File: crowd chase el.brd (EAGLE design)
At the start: 78.7 x 72.4 mm, 27 parts, among them IC2 PIC18F1220P, U4 TRIAC

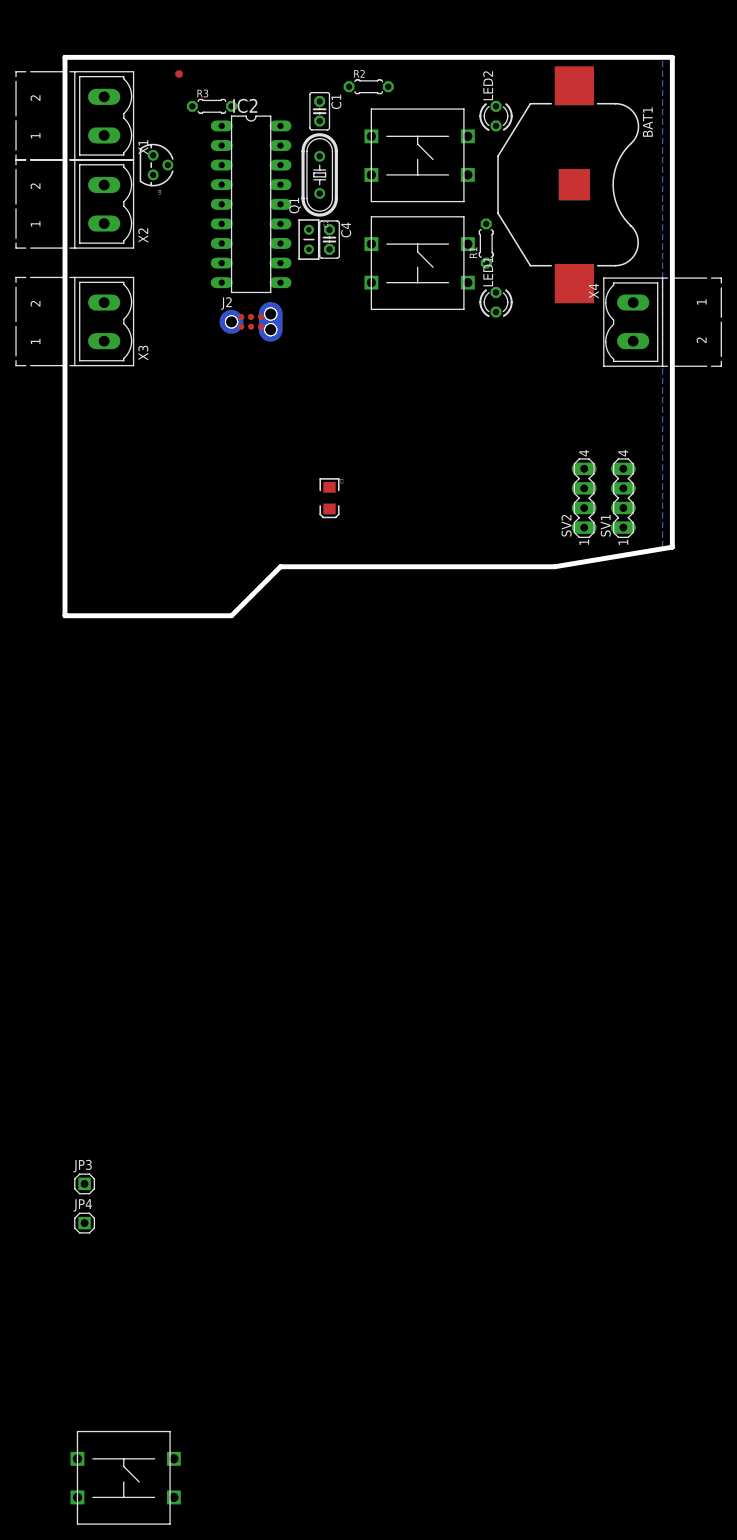
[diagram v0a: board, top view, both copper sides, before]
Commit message: No more airwires
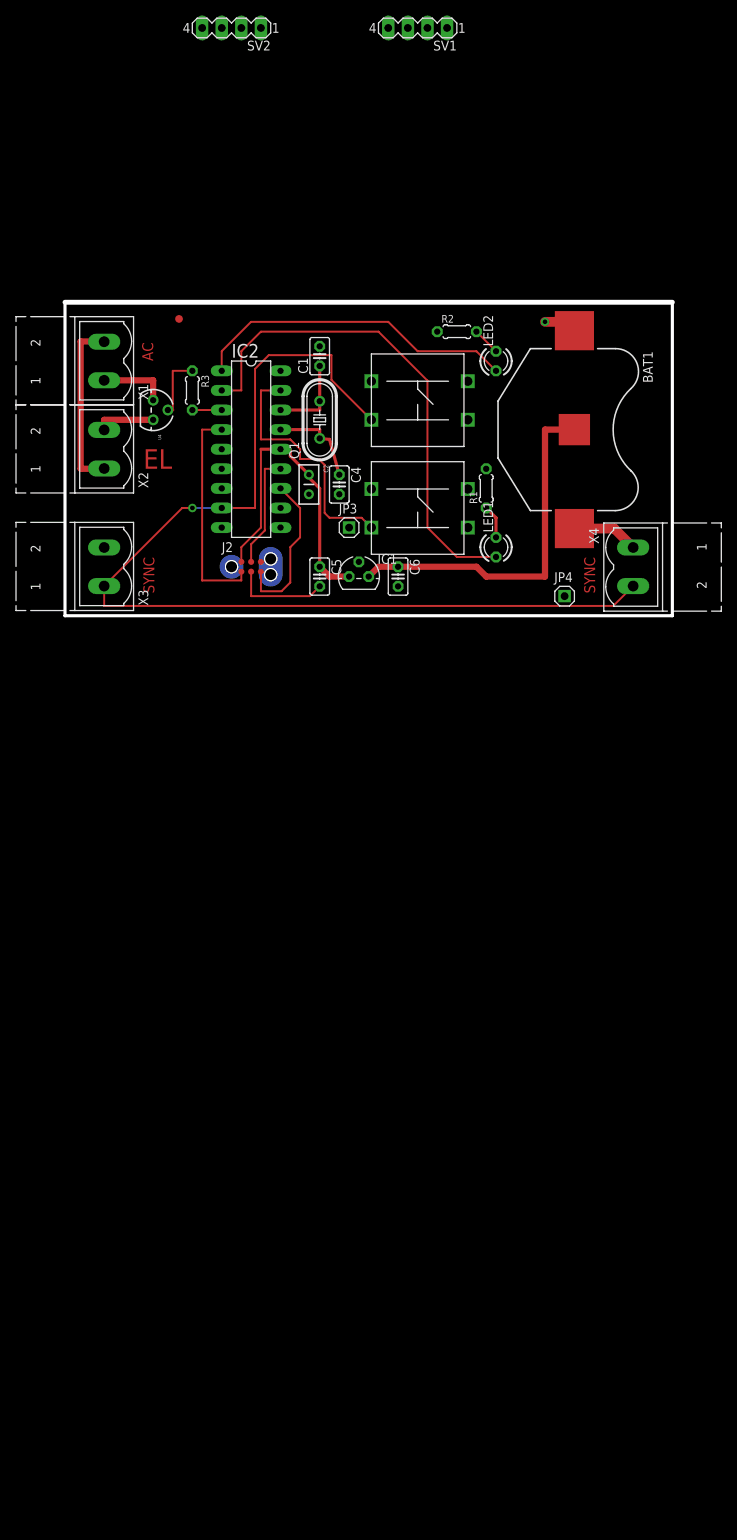
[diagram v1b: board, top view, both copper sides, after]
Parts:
- removed C3: 10uF, SparkFun:EIA3216
- removed U$7: 12MMTACT_MJTP1212, chasetron:MJTP1212
- added C5, C6: 1uF, rcl:C025-025X050
- added IC1: 7805L, linear:TO92
- moved JP4 102.4 mm to (64.8, 2.54)
- moved JP3 91.7 mm to (36.8, 11.4)
- moved SV2 76.2 mm to (21.6, 76.2), turned to 180 degrees
- moved SV1 66.5 mm to (45.7, 76.2), turned to 180 degrees
- moved R3 36.9 mm to (16.5, 29.2), turned to 270 degrees
- moved R2 33.7 mm to (50.8, 36.8)
- moved C4 31.8 mm to (35.6, 17.0)
- moved BAT1 31.8 mm to (66.0, 24.1)
- moved IC2 31.8 mm to (24.1, 21.6)
- moved X2 31.8 mm to (5.08, 21.6)
- moved C1 31.8 mm to (33.0, 33.7), turned to 90 degrees
- moved J2 31.8 mm to (21.6, 6.35)
- moved LED1 31.8 mm to (55.9, 8.89)
- moved Q1 31.8 mm to (33.0, 25.4)
- moved U$6 31.8 mm to (45.7, 14.0)
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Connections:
- new net DEVICE_MAX_SET: IC2.17, U$6.P2A
- new net MAX_LED: IC2.1, LED2.A
- new net N$4: BAT1.2, C6.1, IC1.3
- new net N$8: IC2.9
- new net NUM_LED: IC2.2, LED1.A
- net DEVICE_NUM_SET: now also IC2.8
- net EL_C: now also IC2.3
- net GND: now also C5.2, C6.2, IC1.2, R1.2, R2.1, U$6.P1A; no longer C3.C
- net VDD: now also C5.1, IC1.1, JP3.1; no longer BAT1.2, C3.A
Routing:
- net DEVICE_NUM_SET: track 0.00 -> 135.2 mm, vias 0 -> 1
- net NUM_LED: track 0.00 -> 65.0 mm
- net N$4: track 0.00 -> 46.8 mm
- net MAX_LED: track 0.00 -> 42.3 mm
- net VDD: track 0.00 -> 40.6 mm
- net DEVICE_MAX_SET: track 0.00 -> 32.4 mm
- net N$1: track 0.00 -> 28.3 mm
- net GND: track 0.00 -> 25.0 mm, vias 0 -> 1
- net HV1: track 0.00 -> 22.6 mm
- net ICSP_CLK: track 0.00 -> 20.6 mm
- net ICSP_DATA: track 0.00 -> 14.8 mm
- net N$2: track 0.00 -> 12.2 mm
- net N$3: track 0.00 -> 10.8 mm
- net HVGND1: track 0.00 -> 8.93 mm
- net N$10: track 0.00 -> 8.25 mm
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- removed copper zone on layer 1, net GND
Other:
- board size 78.7 x 72.4 mm -> 78.7 x 40.6 mm
- board text added: "AC"
- board text added: "Blake Robertson"
- board text added: "EL"
- board text added: "SYNC"
- board text removed: "Ryan Owens"

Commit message: v1.0 -- Fabbed Version
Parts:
- added LED3: (no value), led:LED3MM
- added R4: (no value), resistor:0204/5
- added U1: TRIAC, SparkFun:TO-92
- IC1: value 7805L -> REG
- moved SV2 64.1 mm to (6.35, 14.0)
- moved JP4 46.2 mm to (19.1, 8.89)
- moved SV1 38.9 mm to (53.3, 38.1)
- moved JP3 1.80 mm to (35.6, 10.2)
- moved C1 1.42 mm to (34.3, 33.0), turned to 0 degrees
- moved C2 1.27 mm to (31.6, 17.0)
- moved R2 1.27 mm to (50.8, 35.6)
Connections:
- removed net N$4: BAT1.2, C6.1, IC1.3
- new net N$12: SV2.1, U1.3
- new net N$13: SV2.3, U1.1
- new net N$14: IC2.6, U1.2
- new net N$7: IC2.7, LED3.A
- new net N$9: BAT1.3, C6.1, IC1.3
- net GND: now also BAT1.2, LED3.K; no longer BAT1.3
- net N$1: now also R4.1
- net N$8: now also JP4.1
- net VDD: now also R4.2
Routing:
- net N$4: track 46.8 -> 0.00 mm
- net N$9: track 0.00 -> 30.3 mm
- net N$14: track 0.00 -> 14.4 mm, vias 0 -> 2
- net N$13: track 0.00 -> 9.20 mm
- net VDD: track 40.6 -> 49.2 mm
- net N$7: track 0.00 -> 7.62 mm, vias 0 -> 1
- net DEVICE_NUM_SET: track 135.2 -> 142.2 mm
- net HV1: track 22.6 -> 27.7 mm, vias 0 -> 1
- net N$1: track 28.3 -> 32.5 mm
- net N$12: track 0.00 -> 3.07 mm
- net N$8: track 0.00 -> 3.07 mm
- net GND: track 25.0 -> 27.5 mm, vias 1 -> 3
- net HVGND1: track 8.93 -> 10.2 mm, vias 0 -> 1
- net N$3: track 10.8 -> 11.4 mm
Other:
- board text added: "Crowd Chase EL"
